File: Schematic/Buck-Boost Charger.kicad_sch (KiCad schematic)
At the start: 47 parts, among them U11 BQ25756RRVR

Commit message: added sensors?
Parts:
- added C96: 1u, symbol Device:C
- renumbered C108 to C102, C102 to C103, C103 to C104, C104 to C105, C105 to C106, C81 to C76, C80 to C77, C82 to C78, C88 to C79, C83 to C80, C89 to C81, C84 to C82, C90 to C83, C85 to C84, C91 to C85, C92 to C87, C87 to C88, C93 to C89, C94 to C90, C95 to C91, C109 to C92, C106 to C93, C96 to C94, C97 to C95, C98 to C97, C99 to C98, C107 to C99, R122 to R100, R114 to R101, R121 to R102, R118 to R103, R117 to R104, R116 to R105, R115 to R106, R119 to R107, R109 to R95, R113 to R96, R120 to R97, R123 to R98, R124 to R99, U11 to U10
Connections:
- net GND: now also C96.2
- net PPHV: now also C96.1
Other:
- moved on the sheet: C102, C99, R98, R99

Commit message: 1st Schematic Review
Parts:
- renumbered C97 to C100, C98 to C101, C99 to C102, C100 to C103, C101 to C104, C102 to C105, C103 to C106, C104 to C107, C105 to C108, C106 to C109, C76 to C79, C77 to C80, C78 to C81, C79 to C82, C80 to C83, C81 to C84, C82 to C85, C83 to C86, C84 to C87, C85 to C88, C86 to C89, C87 to C90, C88 to C91, C89 to C92, C90 to C93, C91 to C94, C92 to C95, C93 to C96, C94 to C97, C95 to C98, C96 to C99, R98 to R100, R99 to R101, R100 to R102, R101 to R103, R102 to R104, R103 to R105, R104 to R106, R105 to R107, R106 to R108, R107 to R109, R95 to R97, R96 to R98, R97 to R99, U10 to U13

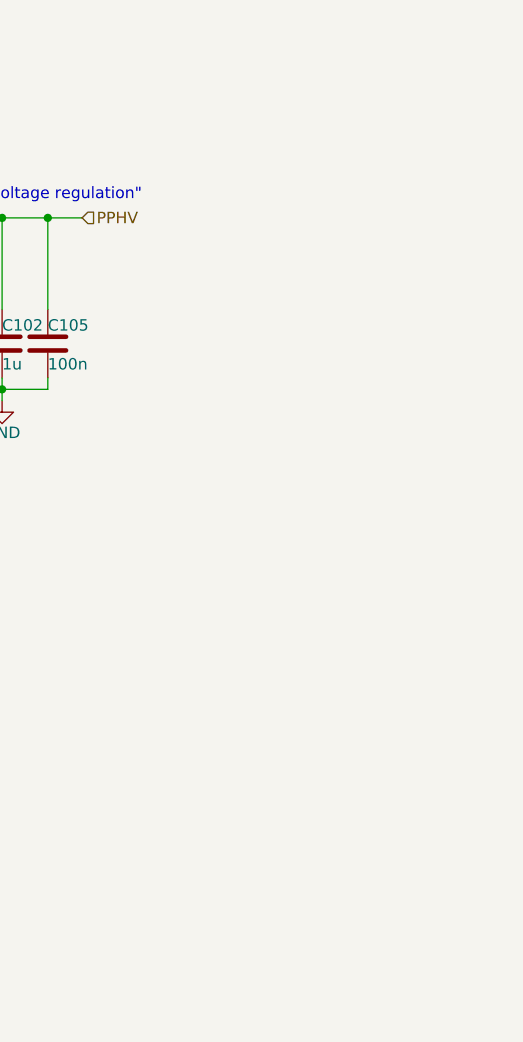
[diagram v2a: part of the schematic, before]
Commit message: added so many test points
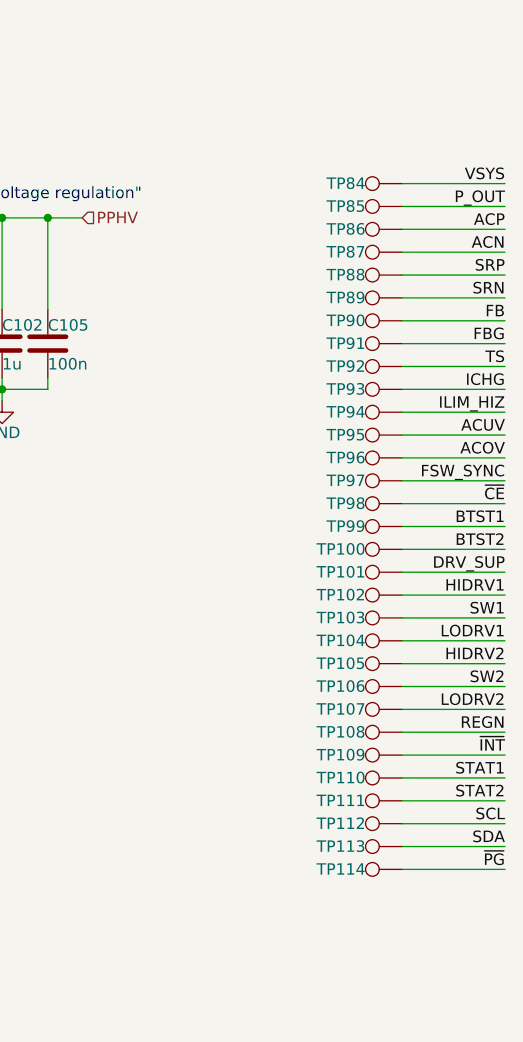
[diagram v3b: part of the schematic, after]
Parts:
- added TP100, TP101, TP102, TP103, TP104, TP105, TP106, TP107, TP108, TP109, TP110, TP111, TP112, TP113, TP114, TP84, TP85, TP86, TP87, TP88, TP89, TP90, TP91, TP92, TP93, TP94, TP95, TP96, TP97, TP98, TP99: TestPoint, symbol Connector:TestPoint
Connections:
- net ACN: now also TP87.1
- net ACOV: now also TP96.1
- net ACP: now also TP86.1
- net ACUV: now also TP95.1
- net BTST1: now also TP99.1
- net BTST2: now also TP100.1
- net DRV_SUP: now also TP101.1
- net FB: now also TP90.1
- net FBG: now also TP91.1
- net FSW_SYNC: now also TP97.1
- net HIDRV1: now also TP102.1
- net HIDRV2: now also TP105.1
- net ICHG: now also TP93.1
- net ILIM_HIZ: now also TP94.1
- net LODRV1: now also TP104.1
- net LODRV2: now also TP107.1
- net P_OUT: now also TP85.1
- net REGN: now also TP108.1
- net SCL: now also TP112.1
- net SDA: now also TP113.1
- net SRN: now also TP89.1
- net SRP: now also TP88.1
- net STAT1: now also TP110.1
- net STAT2: now also TP111.1
- net SW1: now also TP103.1
- net SW2: now also TP106.1
- net TS: now also TP92.1
- net VSYS: now also TP84.1
- net ~{CE}: now also TP98.1
- net ~{INT}: now also TP109.1
- net ~{PG}: now also TP114.1

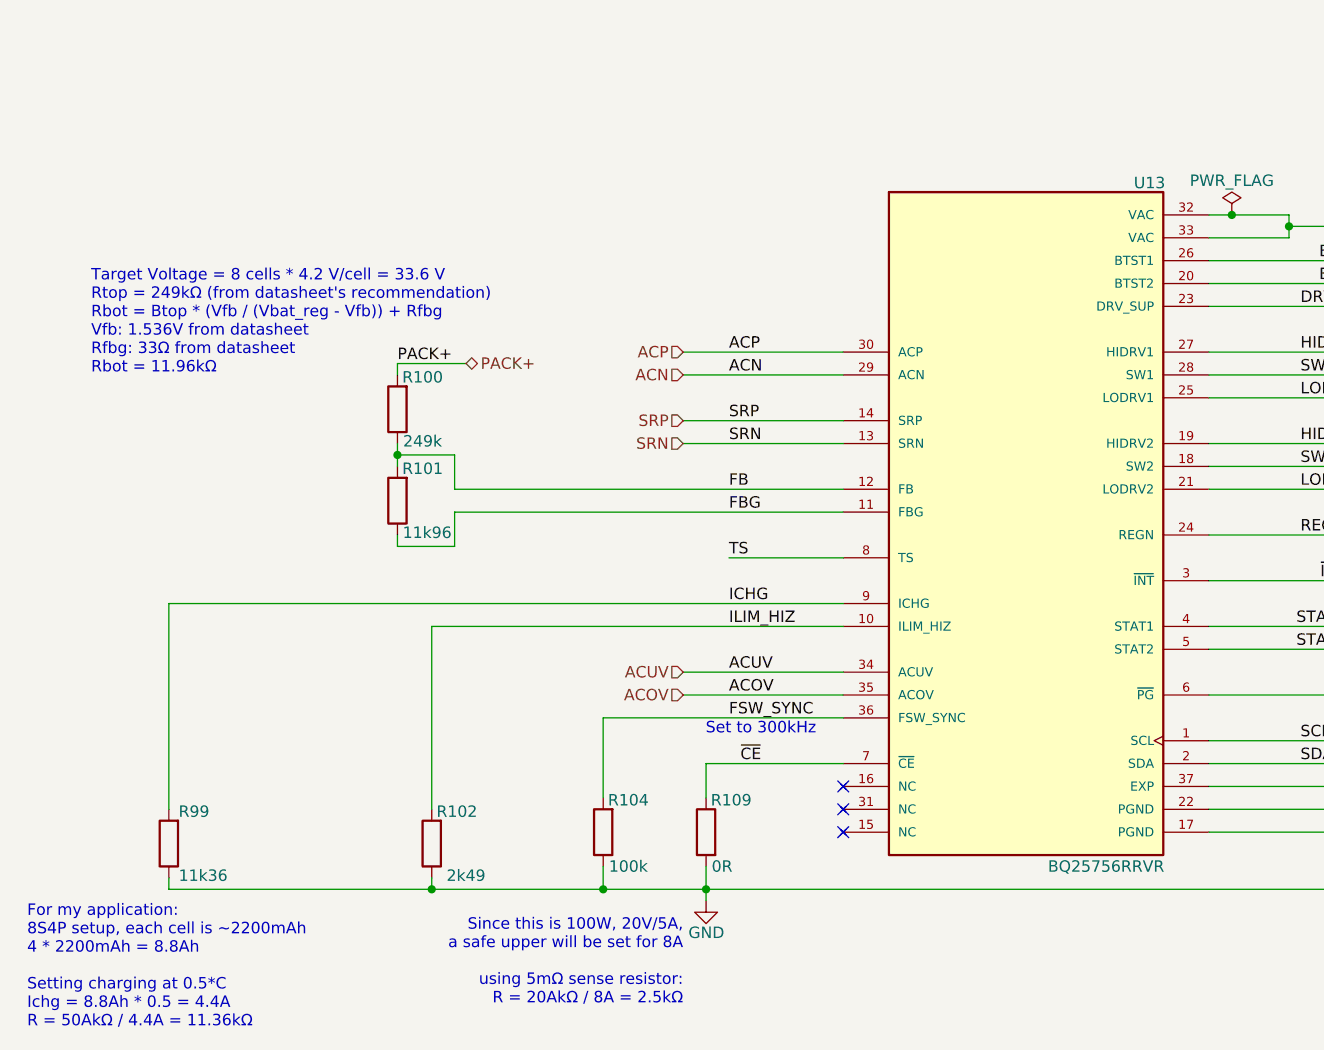
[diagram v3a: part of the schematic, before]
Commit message: fixed power lines
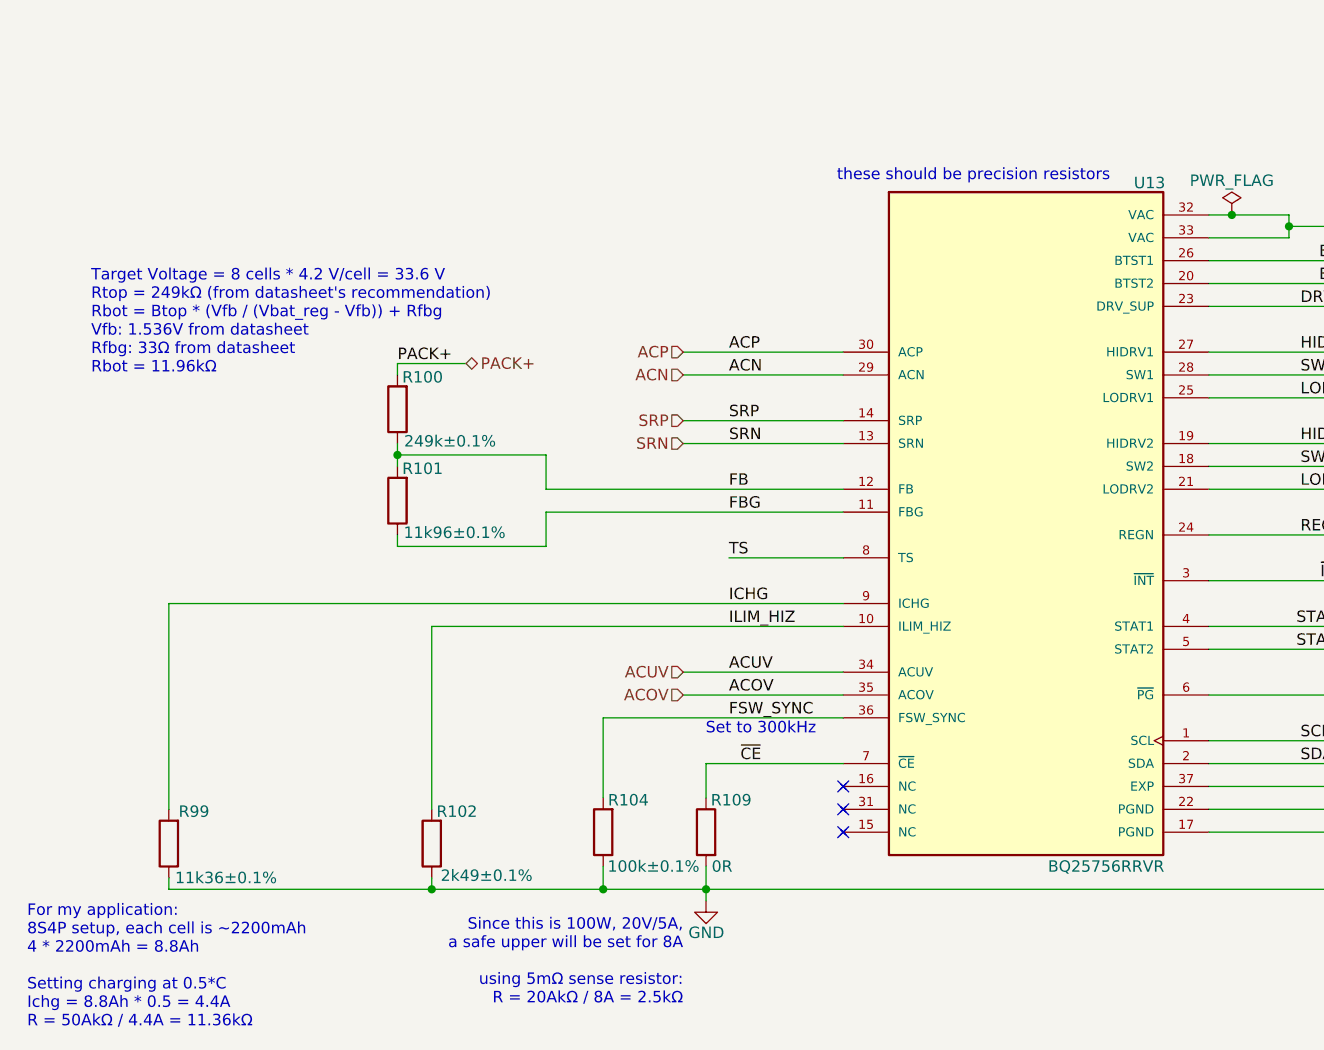
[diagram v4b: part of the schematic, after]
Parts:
- R100: value 249k -> 249k±0.1%
- R101: value 11k96 -> 11k96±0.1%
- R102: value 2k49 -> 2k49±0.1%
- R104: value 100k -> 100k±0.1%
- R99: value 11k36 -> 11k36±0.1%
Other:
- note added: "these should be precision resistors"
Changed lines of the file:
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@@
 		)
 	)
+	(text "these should be precision resistors"
+		(exclude_from_sim no)
+		(at 124.968 80.772 0)
+		(effects
+			(font
+				(size 1.27 1.27)
+			)
+		)
+	)
 	(text "For my application:\n8S4P setup, each cell is ~2200mAh\n4 * 2200mAh = 8.8Ah\n\nSetting charging at 0.5*C\nIchg = 8.8Ah * 0.5 = 4.4A\nR = 50AkΩ / 4.4A = 11.36kΩ"
 		(exclude_from_sim no)
@@
 	(wire
 		(pts
-			(xy 67.31 115.57) (xy 67.31 111.76)
+			(xy 77.47 115.57) (xy 77.47 111.76)
 		)
 		(stroke
@@
 	(wire
 		(pts
-			(xy 67.31 118.11) (xy 110.49 118.11)
+			(xy 77.47 118.11) (xy 110.49 118.11)
 		)
 		(stroke
@@
 	(wire
 		(pts
-			(xy 67.31 111.76) (xy 60.96 111.76)
+			(xy 77.47 111.76) (xy 60.96 111.76)
 		)
 		(stroke
@@
 	(wire
 		(pts
-			(xy 67.31 118.11) (xy 67.31 121.92)
+			(xy 77.47 118.11) (xy 77.47 121.92)
 		)
 		(stroke
@@
 	(wire
 		(pts
-			(xy 67.31 115.57) (xy 110.49 115.57)
+			(xy 77.47 115.57) (xy 110.49 115.57)
 		)
 		(stroke
@@
 	(wire
 		(pts
-			(xy 67.31 121.92) (xy 60.96 121.92)
+			(xy 77.47 121.92) (xy 60.96 121.92)
 		)
 		(stroke
@@
 			)
 		)
-		(property "Value" "249k"
-			(at 63.754 110.236 0)
+		(property "Value" "249k±0.1%"
+			(at 66.802 110.236 0)
 			(effects
 				(font
@@
 			)
 		)
-		(property "Value" "11k36"
-			(at 39.37 158.496 0)
+		(property "Value" "11k36±0.1%"
+			(at 41.91 158.75 0)
 			(effects
 				(font
@@
 			)
 		)
-		(property "Value" "2k49"
-			(at 68.58 158.496 0)
+		(property "Value" "2k49±0.1%"
+			(at 70.866 158.496 0)
 			(effects
 				(font
@@
 			)
 		)
-		(property "Value" "100k"
-			(at 86.614 157.48 0)
+		(property "Value" "100k±0.1%"
+			(at 89.408 157.48 0)
 			(effects
 				(font
@@
 			)
 		)
-		(property "Value" "11k96"
-			(at 64.262 120.396 0)
+		(property "Value" "11k96±0.1%"
+			(at 67.31 120.396 0)
 			(effects
 				(font

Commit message: updates
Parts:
- renumbered D41 to D43, D42 to D44, R97 to R102, R98 to R103, R99 to R104, R100 to R105, R101 to R106, R102 to R107, R103 to R108, R104 to R109, R105 to R110, R106 to R111, R107 to R112, R108 to R113, R109 to R114
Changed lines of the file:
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@@
 		(on_board yes)
 		(dnp no)
-		(property "Reference" "R108"
+		(property "Reference" "R113"
 			(at 83.566 52.324 90)
 			(effects
@@
 			(project "STAR"
 				(path "/fc8533bc-25dd-4c20-9b4c-ffebebd6739b/ec72a35b-e7f2-4422-8859-60e9fb848154/6f9fe965-58a5-4a06-b6b6-8090ff5dc05f"
-					(reference "R108")
+					(reference "R113")
 					(unit 1)
 				)
@@
 		(on_board yes)
 		(dnp no)
-		(property "Reference" "D42"
+		(property "Reference" "D44"
 			(at 89.916 33.02 0)
 			(effects
@@
 			(project "STAR"
 				(path "/fc8533bc-25dd-4c20-9b4c-ffebebd6739b/ec72a35b-e7f2-4422-8859-60e9fb848154/6f9fe965-58a5-4a06-b6b6-8090ff5dc05f"
-					(reference "D42")
+					(reference "D44")
 					(unit 1)
 				)
@@
 		(on_board yes)
 		(dnp no)
-		(property "Reference" "R100"
+		(property "Reference" "R105"
 			(at 63.754 103.124 0)
 			(effects
@@
 			(project "STAR"
 				(path "/fc8533bc-25dd-4c20-9b4c-ffebebd6739b/ec72a35b-e7f2-4422-8859-60e9fb848154/6f9fe965-58a5-4a06-b6b6-8090ff5dc05f"
-					(reference "R100")
+					(reference "R105")
 					(unit 1)
 				)
@@
 		(on_board yes)
 		(dnp no)
-		(property "Reference" "R106"
+		(property "Reference" "R111"
 			(at 83.82 47.244 90)
 			(effects
@@
 			(project "STAR"
 				(path "/fc8533bc-25dd-4c20-9b4c-ffebebd6739b/ec72a35b-e7f2-4422-8859-60e9fb848154/6f9fe965-58a5-4a06-b6b6-8090ff5dc05f"
-					(reference "R106")
+					(reference "R111")
 					(unit 1)
 				)
@@
 		(on_board yes)
 		(dnp no)
-		(property "Reference" "R99"
+		(property "Reference" "R104"
 			(at 38.354 151.384 0)
 			(effects
@@
 			(project "STAR"
 				(path "/fc8533bc-25dd-4c20-9b4c-ffebebd6739b/ec72a35b-e7f2-4422-8859-60e9fb848154/6f9fe965-58a5-4a06-b6b6-8090ff5dc05f"
-					(reference "R99")
+					(reference "R104")
 					(unit 1)
 				)
@@
 		(on_board yes)
 		(dnp no)
-		(property "Reference" "R102"
+		(property "Reference" "R107"
 			(at 67.564 151.384 0)
 			(effects
@@
 			(project "STAR"
 				(path "/fc8533bc-25dd-4c20-9b4c-ffebebd6739b/ec72a35b-e7f2-4422-8859-60e9fb848154/6f9fe965-58a5-4a06-b6b6-8090ff5dc05f"
-					(reference "R102")
+					(reference "R107")
 					(unit 1)
 				)
@@
 		(on_board yes)
 		(dnp no)
-		(property "Reference" "R97"
+		(property "Reference" "R102"
 			(at 38.354 25.654 0)
 			(effects
@@
 			(project "STAR"
 				(path "/fc8533bc-25dd-4c20-9b4c-ffebebd6739b/ec72a35b-e7f2-4422-8859-60e9fb848154/6f9fe965-58a5-4a06-b6b6-8090ff5dc05f"
-					(reference "R97")
+					(reference "R102")
 					(unit 1)
 				)
@@
 		(on_board yes)
 		(dnp no)
-		(property "Reference" "R98"
+		(property "Reference" "R103"
 			(at 38.354 37.084 0)
 			(effects
@@
 			(project "STAR"
 				(path "/fc8533bc-25dd-4c20-9b4c-ffebebd6739b/ec72a35b-e7f2-4422-8859-60e9fb848154/6f9fe965-58a5-4a06-b6b6-8090ff5dc05f"
-					(reference "R98")
+					(reference "R103")
 					(unit 1)
 				)
@@
 		(on_board yes)
 		(dnp no)
-		(property "Reference" "R103"
+		(property "Reference" "R108"
 			(at 64.262 48.514 90)
 			(effects
@@
 			(project "STAR"
 				(path "/fc8533bc-25dd-4c20-9b4c-ffebebd6739b/ec72a35b-e7f2-4422-8859-60e9fb848154/6f9fe965-58a5-4a06-b6b6-8090ff5dc05f"
-					(reference "R103")
+					(reference "R108")
 					(unit 1)
 				)
@@
 		(on_board yes)
 		(dnp no)
-		(property "Reference" "R104"
+		(property "Reference" "R109"
 			(at 86.614 150.114 0)
 			(effects
@@
 			(project "STAR"
 				(path "/fc8533bc-25dd-4c20-9b4c-ffebebd6739b/ec72a35b-e7f2-4422-8859-60e9fb848154/6f9fe965-58a5-4a06-b6b6-8090ff5dc05f"
-					(reference "R104")
+					(reference "R109")
 					(unit 1)
 				)
@@
 		(on_board yes)
 		(dnp no)
-		(property "Reference" "R107"
+		(property "Reference" "R112"
 			(at 83.566 49.784 90)
 			(effects
@@
 			(project "STAR"
 				(path "/fc8533bc-25dd-4c20-9b4c-ffebebd6739b/ec72a35b-e7f2-4422-8859-60e9fb848154/6f9fe965-58a5-4a06-b6b6-8090ff5dc05f"
-					(reference "R107")
+					(reference "R112")
 					(unit 1)
 				)
@@
 		(on_board yes)
 		(dnp no)
-		(property "Reference" "R105"
+		(property "Reference" "R110"
 			(at 83.566 44.704 90)
 			(effects
@@
 			(project "STAR"
 				(path "/fc8533bc-25dd-4c20-9b4c-ffebebd6739b/ec72a35b-e7f2-4422-8859-60e9fb848154/6f9fe965-58a5-4a06-b6b6-8090ff5dc05f"
-					(reference "R105")
+					(reference "R110")
 					(unit 1)
 				)
@@
 		(on_board yes)
 		(dnp no)
-		(property "Reference" "R101"
+		(property "Reference" "R106"
 			(at 63.754 113.284 0)
 			(effects
@@
 			(project "STAR"
 				(path "/fc8533bc-25dd-4c20-9b4c-ffebebd6739b/ec72a35b-e7f2-4422-8859-60e9fb848154/6f9fe965-58a5-4a06-b6b6-8090ff5dc05f"
-					(reference "R101")
+					(reference "R106")
 					(unit 1)
 				)
@@
 		(on_board yes)
 		(dnp no)
-		(property "Reference" "D41"
+		(property "Reference" "D43"
 			(at 67.056 33.02 0)
 			(effects
@@
 			(project "STAR"
 				(path "/fc8533bc-25dd-4c20-9b4c-ffebebd6739b/ec72a35b-e7f2-4422-8859-60e9fb848154/6f9fe965-58a5-4a06-b6b6-8090ff5dc05f"
-					(reference "D41")
+					(reference "D43")
 					(unit 1)
 				)
@@
 		(on_board yes)
 		(dnp no)
-		(property "Reference" "R109"
+		(property "Reference" "R114"
 			(at 98.044 150.114 0)
 			(effects
@@
 			(project "STAR"
 				(path "/fc8533bc-25dd-4c20-9b4c-ffebebd6739b/ec72a35b-e7f2-4422-8859-60e9fb848154/6f9fe965-58a5-4a06-b6b6-8090ff5dc05f"
-					(reference "R109")
+					(reference "R114")
 					(unit 1)
 				)
